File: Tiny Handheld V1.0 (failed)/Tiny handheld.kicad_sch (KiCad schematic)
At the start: 41 parts, among them IC1 BQ21040DBVR, J1 VDisplay/prog1, J2 HDisplay/prog, J3 USB_C_Receptacle_USB2.0, U1 ATtiny85-20P, U2 ATtiny85-20S

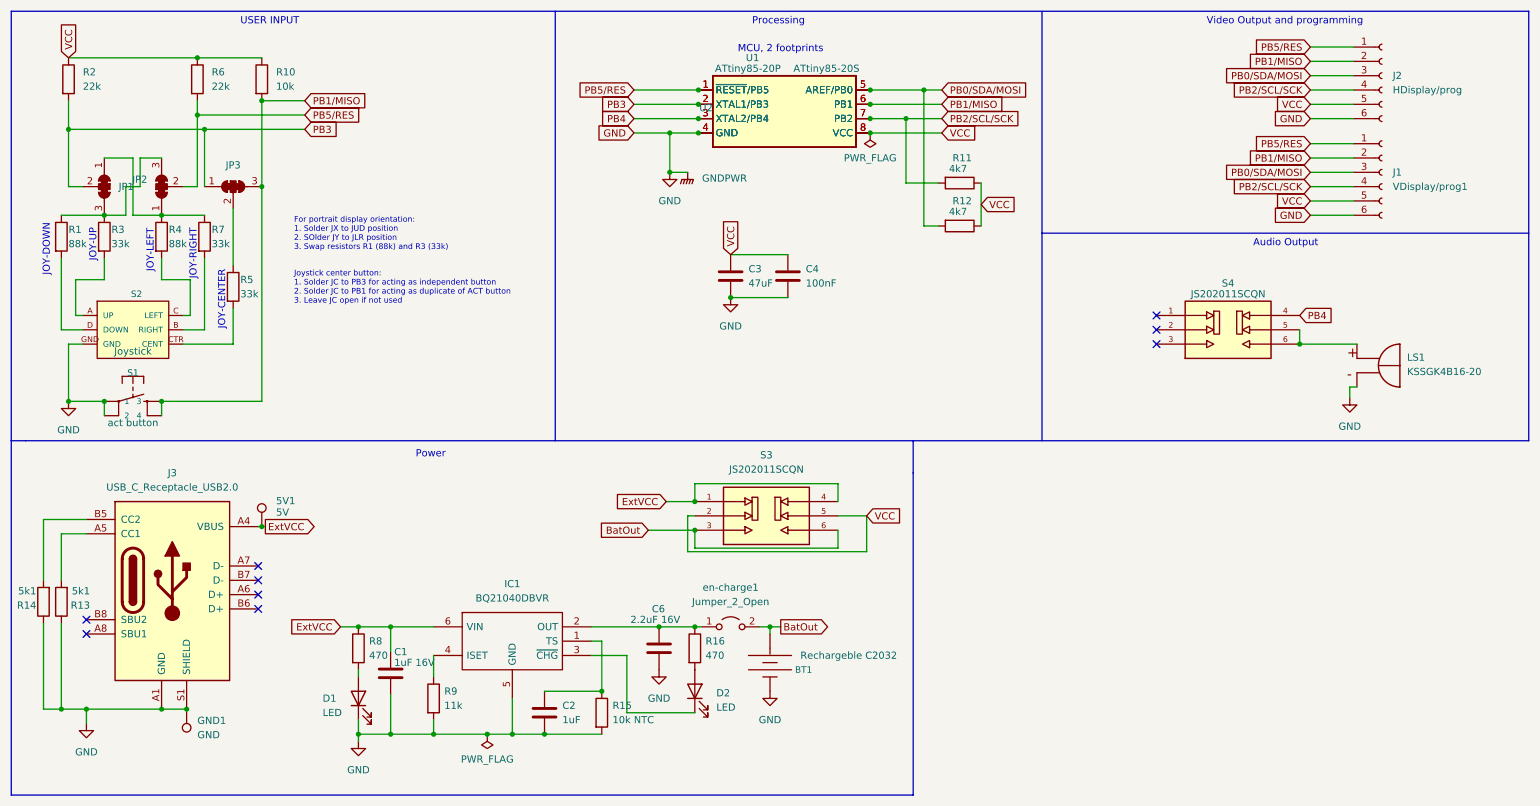
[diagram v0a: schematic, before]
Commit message: Added V1.0 and v2.0 seperately
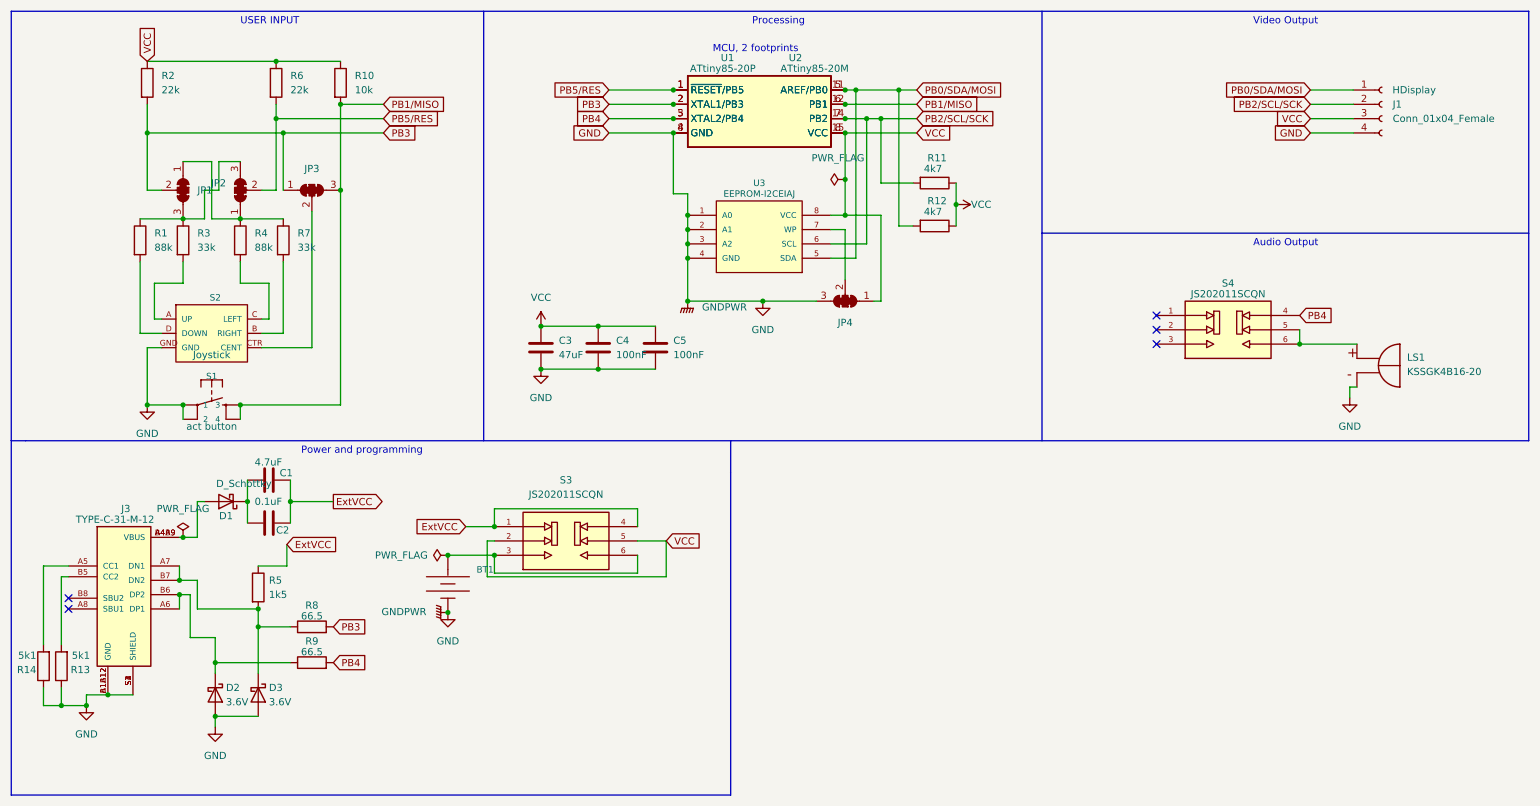
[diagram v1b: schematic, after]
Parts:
- removed 5V1: 5V, TestPoint:TestPoint_Pad_1.0x1.0mm, symbol Connector:TestPoint
- removed C6: 2.2uF 16V, Capacitor_SMD:C_1206_3216Metric_Pad1.33x1.80mm_HandSolder, symbol Device:C
- removed D1, D2: LED, LED_SMD:LED_1206_3216Metric_Pad1.42x1.75mm_HandSolder, symbol Device:LED
- removed GND1: GND, TestPoint:TestPoint_Pad_1.0x1.0mm, symbol Connector:TestPoint
- removed IC1: BQ21040DBVR, Package_TO_SOT_SMD:SOT-23-6_Handsoldering, symbol SamacSys_Parts:BQ21040DBVR
- removed J1: VDisplay/prog1, Connector_PinSocket_2.54mm:PinSocket_1x06_P2.54mm_Vertical, symbol Connector:Conn_01x06_Female
- removed J2: HDisplay/prog, Connector_PinSocket_2.54mm:PinSocket_1x06_P2.54mm_Vertical, symbol Connector:Conn_01x06_Female
- removed J3: USB_C_Receptacle_USB2.0, USB-C-Power-tester:TYPE-C-31-M-17_handsolder, symbol Connector:USB_C_Receptacle_USB2.0
- removed R15: 10k NTC, Resistor_SMD:R_1206_3216Metric_Pad1.30x1.75mm_HandSolder, symbol Device:R
- removed R16: 470, Resistor_SMD:R_1206_3216Metric_Pad1.30x1.75mm_HandSolder, symbol Device:R
- removed U2: ATtiny85-20S, Package_SO:SOIC-8W_5.3x5.3mm_P1.27mm, symbol MCU_Microchip_ATtiny:ATtiny85-20S
- removed en-charge1: Jumper_2_Open, Jumper:SolderJumper-2_P1.3mm_Open_RoundedPad1.0x1.5mm, symbol Jumper:Jumper_2_Open
- added C5: 100nF, Capacitor_SMD:C_1206_3216Metric_Pad1.33x1.80mm_HandSolder, symbol Device:C
- added D1: D_Schottky, Diode_SMD:D_1210_3225Metric_Pad1.42x2.65mm_HandSolder, symbol Device:D_Schottky
- added D2, D3: 3.6V, Diode_SMD:D_1210_3225Metric_Pad1.42x2.65mm_HandSolder, symbol Device:D_Schottky
- added J1: Conn_01x04_Female, Connector_PinHeader_2.54mm:PinHeader_1x04_P2.54mm_Vertical, symbol Connector:Conn_01x04_Female
- added J3: TYPE-C-31-M-12, Snapeda:HRO_TYPE-C-31-M-12, symbol TYPE-C-31-M-12:TYPE-C-31-M-12
- added JP4: SolderJumper_3_Bridged123, Jumper:SolderJumper-3_P1.3mm_Open_RoundedPad1.0x1.5mm_NumberLabels, symbol Jumper:SolderJumper_3_Bridged123
- added U2: ATtiny85-20M, Snapeda:QFN50P400X400X80-21N, symbol MCU_Microchip_ATtiny:ATtiny85-20M
- added U3: EEPROM-I2CEIAJ, Package_SO:SOIC-8_3.9x4.9mm_P1.27mm, symbol SparkFun-IC-Memory:EEPROM-I2CEIAJ
- BT1: footprint Battery:BatteryHolder_Keystone_3002_1x2032 -> Snapeda:BAT_BU2032-1; Purpose Rechargeble C2032 -> (none)
- C1: value 1uF 16V -> 4.7uF
- C2: value 1uF -> 0.1uF
- R5: value 33k -> 1k5
- R8: value 470 -> 66.5
- R9: value 11k -> 66.5
- U1: footprint SamacSys_Parts:DIP781W56P254L950H533Q8N -> Package_DIP:DIP-8_W7.62mm
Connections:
- net ExtVCC: now also C2.1, R5.1; no longer R8.1
- net GND: now also C5.2, D2.2 (A), D3.2 (A), J1.4 (Pin_4), J3.A1B12 (GND), J3.B1A12 (GND), J3.S1 (SHIELD), J3.S2 (SHIELD), J3.S3 (SHIELD), J3.S4 (SHIELD), JP4.3 (B), U2.21 (GND), U2.8 (GND), U3.1 (A0), U3.2 (A1), U3.3 (A2), U3.4 (GND); no longer C1.2, C2.2, R9.2
- net PB0/SDA/MOSI: now also J1.1 (Pin_1), U2.11 (AREF/PB0), U3.5 (SDA)
- net PB1/MISO: now also U2.12 (PB1)
- net PB2/SCL/SCK: now also J1.2 (Pin_2), U2.14 (PB2), U3.6 (SCL)
- net PB3: now also R8.2, U2.2 (XTAL1/PB3)
- net PB4: now also R9.2, U2.5 (XTAL2/PB4)
- net PB5/RES: now also U2.1 (~{RESET}/PB5)
- net VCC: now also C5.1, J1.3 (Pin_3), JP4.1 (A), U2.15 (VCC), U3.8 (VCC)
- net at JP3.2 (C): now also S2.CTR (CENT); no longer R5.1
- net at R5.2: now also R8.1, D3.1 (K), J3.A7 (DN1), J3.B7 (DN2); no longer S2.CTR (CENT)
- net at R14.2: now also J3.A5 (CC1)
- net at R9.1: now also D2.1 (K), J3.A6 (DP1), J3.B6 (DP2)
- net at R13.2: now also J3.B5 (CC2)
- net BatOut: no longer names the net of BT1.+, S3.3, S3.6
- new net: D1.2 (A), J3.A4B9 (VBUS), J3.B4A9 (VBUS)
- new net: JP4.2 (C), U3.7 (WP)
- new net: C1.2, C2.2, D1.1 (K)
- no-connect marks 9 -> 5
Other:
- note added: "Power and programming"
- note added: "Video Output"
- note removed: "For portrait display orientation: 1. Solder JX to JUD position 2. SOlder JY to JLR position 3. Swap resistors R1 (88k) and R3 (33k)"
- note removed: "JOY-CENTER"
- note removed: "JOY-DOWN"
- note removed: "JOY-LEFT"
- note removed: "JOY-RIGHT"
- note removed: "JOY-UP"
- note removed: "Joystick center button: 1. Solder JC to PB3 for acting as independent button 2. Solder JC to PB1 for acting as duplicate of ACT button 3. Leave JC open if not used"
- note removed: "Power"
- note removed: "Video Output and programming"
- moved on the sheet: BT1, C3, C4, JP1, JP2, JP3, R1, R10, R11, R12, R13, R14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
